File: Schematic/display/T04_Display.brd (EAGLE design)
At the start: 76.3 x 50.8 mm, 46 parts

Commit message: Reverified ERC/DRC for assignment files, added version summery.
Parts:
- C1, C10, C11, C12, C13, C14, C2, C3, C4, C5, C6, C7, C8, C9: value (none) -> 0.1u
- LED1, LED4, LED7: value (none) -> G
- LED2, LED5, LED8: value (none) -> Y
- LED3, LED6, LED9: value (none) -> R
- R1, R2, R3, R4, R5, R6, R7, R8, R9: value (none) -> 150

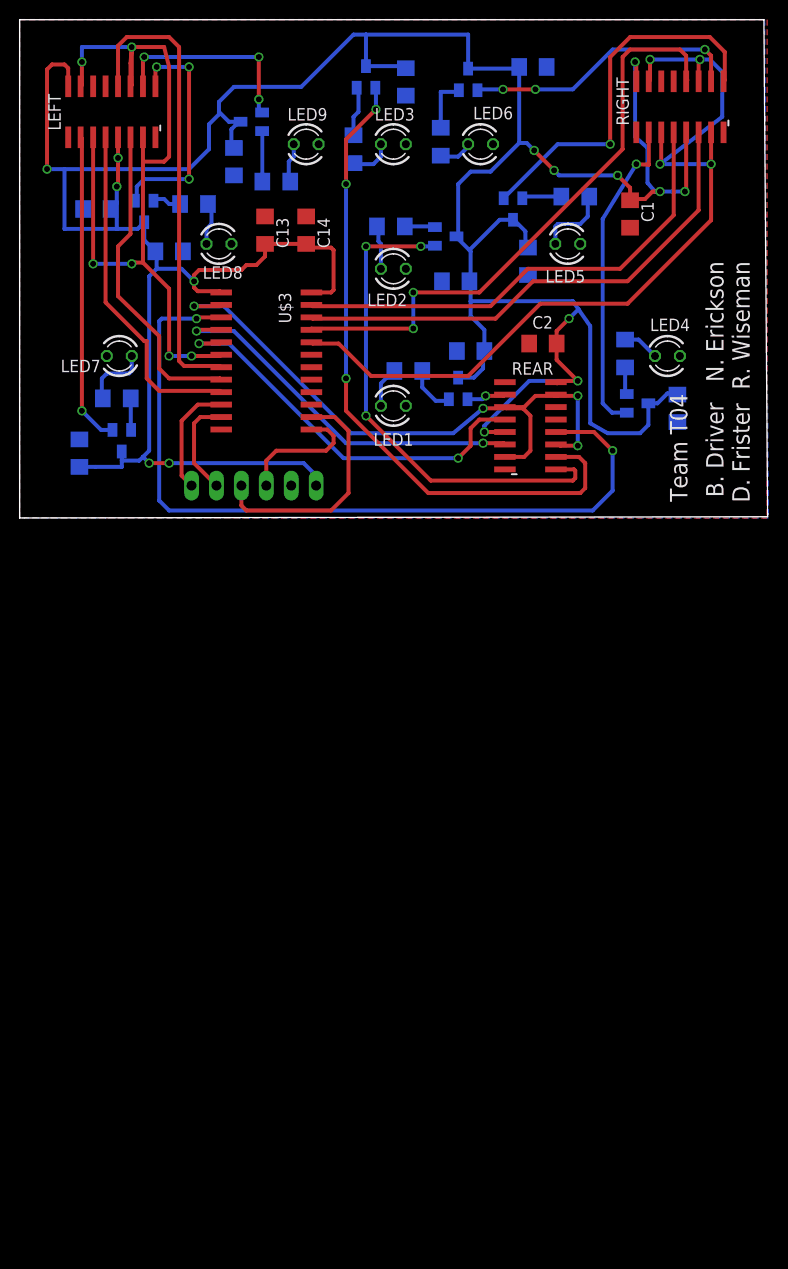
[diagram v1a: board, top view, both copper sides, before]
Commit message: Mainboard & Display layout updates - Molex connectors, Mounting Holes, Greenberg Email Additions
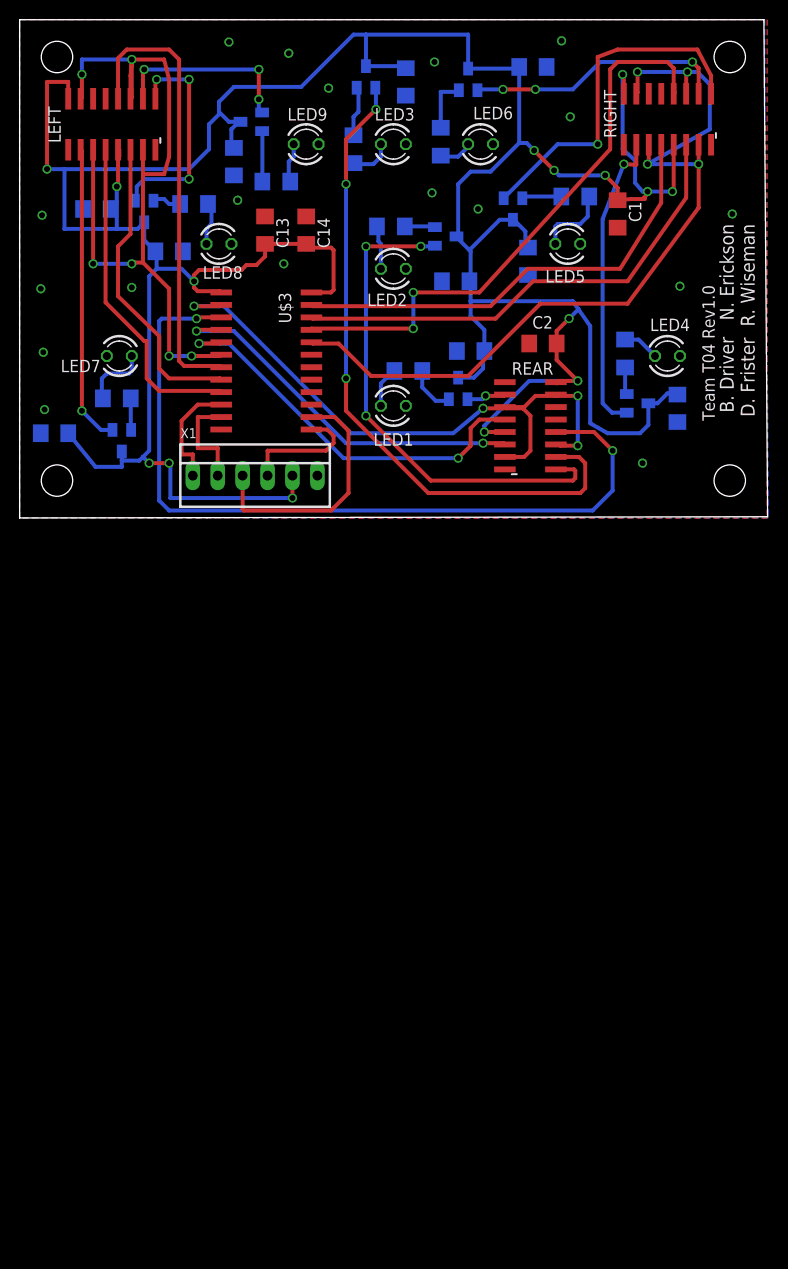
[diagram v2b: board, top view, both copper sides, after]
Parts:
- removed SV1: Connector, con-lstb:MA06-1
- added X1: (no value), con-molex:22-23-2061
- moved C12 3.25 mm to (3.56, 8.64), turned to 0 degrees
- moved RIGHT 1.80 mm to (66.0, 40.6)
- moved LEFT 1.27 mm to (9.40, 40.1)
- moved C1 1.27 mm to (61.0, 31.0)
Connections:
- net A0: now also X1.1; no longer SV1.6
- net A1: now also X1.2; no longer SV1.5
- net A2: now also X1.3; no longer SV1.4
- net A3: now also X1.4; no longer SV1.3
- net GND: now also X1.6; no longer SV1.2
- net VDD: now also X1.5; no longer SV1.1
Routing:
- net RRES: track 91.3 -> 86.9 mm
- net BRES: track 81.4 -> 78.7 mm
- net RS2: track 52.0 -> 49.7 mm
- net RS1: track 49.3 -> 46.9 mm
- net RY: track 38.2 -> 35.9 mm
- net RS3: track 60.8 -> 58.7 mm
- net RG: track 32.8 -> 30.9 mm
- net RR: track 28.4 -> 26.6 mm
- net VDD: track 348.9 -> 347.2 mm
- net BS1: track 34.6 -> 33.4 mm
- net BG: track 31.9 -> 30.6 mm
- net BS2: track 32.7 -> 31.4 mm
- net BR: track 20.5 -> 19.2 mm
- net BS3: track 47.7 -> 46.4 mm
- net BY: track 23.9 -> 22.7 mm
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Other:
- board text added: "Team T04 Rev1.0"
- board text removed: "Team T04"

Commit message: Updated Schematic and Revision text to match instructor review.
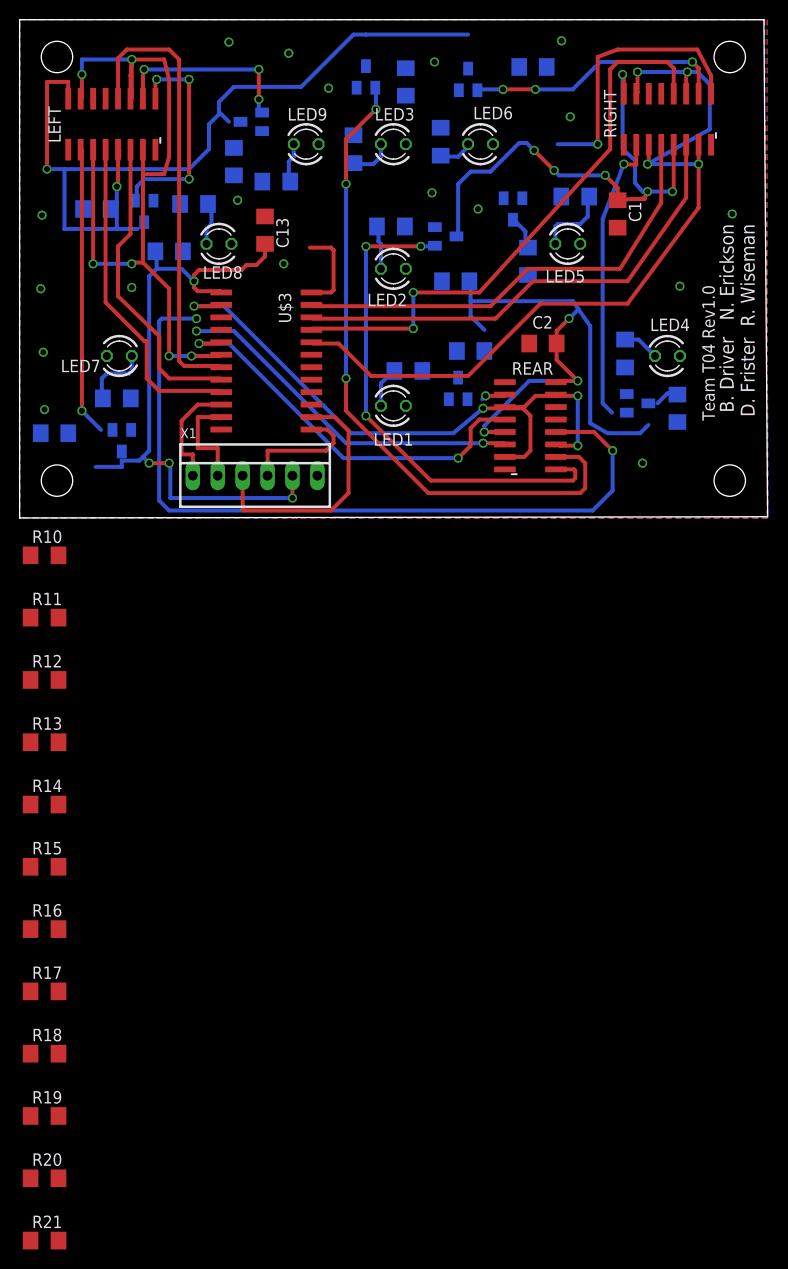
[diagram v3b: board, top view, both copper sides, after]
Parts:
- removed C14: 0.1u, resistor:C1206
- added R10, R11, R12, R13, R14, R15, R16, R17, R18, R19, R20, R21: 4700, rcl:R1206
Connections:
- removed net N$11: R7.2, U$9.2
- removed net N$2: R8.2, U$8.2
- removed net N$7: R9.2, U$6.2
- new net N$21: LED6.K, U$9.3
- new net N$22: LED4.K, U$6.3
- new net N$23: LED5.K, U$8.3
- net BRES: now also R18.2
- net BS1: now also R21.2
- net BS2: now also R20.2
- net BS3: now also R19.2
- net GND: now also R10.1, R11.1, R12.1, R13.1, R14.1, R15.1, R16.1, R17.1, R18.1, R19.1, R20.1, R21.1, U$1.2, U$10.2, U$12.2, U$13.2, U$4.2, U$5.2, U$6.2, U$8.2, U$9.2; no longer C14.1, LED1.K, LED2.K, LED3.K, LED4.K, LED5.K, LED6.K, LED7.K, LED8.K, LED9.K
- net LRES: now also R14.2
- net LS1: now also R17.2
- net LS2: now also R16.2
- net LS3: now also R15.2
- net N$1: now also LED3.K, U$5.3; no longer R5.2, U$4.2
- net N$13: now also LED7.K, U$10.3; no longer R1.2, U$10.2
- net N$15: now also LED8.K, U$12.3; no longer R2.2, U$12.2
- net N$17: now also LED9.K, U$13.3; no longer R3.2, U$13.2
- net N$3: now also LED2.K, U$4.3; no longer R6.2, U$5.2
- net N$4: now also LED1.K, U$1.3; no longer R4.2, U$1.2
- net RRES: now also R13.2
- net RS1: now also R10.2
- net RS2: now also R11.2
- net RS3: now also R12.2
- net VDD: now also R1.2, R2.2, R3.2, R4.2, R5.2, R6.2, R7.2, R8.2, R9.2; no longer C14.2, U$1.3, U$10.3, U$12.3, U$13.3, U$4.3, U$5.3, U$6.3, U$8.3, U$9.3
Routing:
- net VDD: track 347.2 -> 283.0 mm
- net RY: track 35.9 -> 28.1 mm
- net N$11: track 5.57 -> 0.00 mm
- net N$17: track 5.15 -> 0.00 mm
- net N$3: track 5.13 -> 0.00 mm
- net N$4: track 5.02 -> 0.00 mm
- net N$2: track 4.05 -> 0.00 mm
- net N$13: track 3.23 -> 0.00 mm
- net N$1: track 3.09 -> 0.00 mm
- net N$15: track 2.99 -> 0.00 mm
- net N$7: track 2.78 -> 0.00 mm
- net LS2: track 38.8 -> 36.4 mm
- net LS3: track 82.9 -> 80.5 mm
- net RG: track 30.9 -> 29.4 mm
- net LG: track 4.01 -> 2.50 mm
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
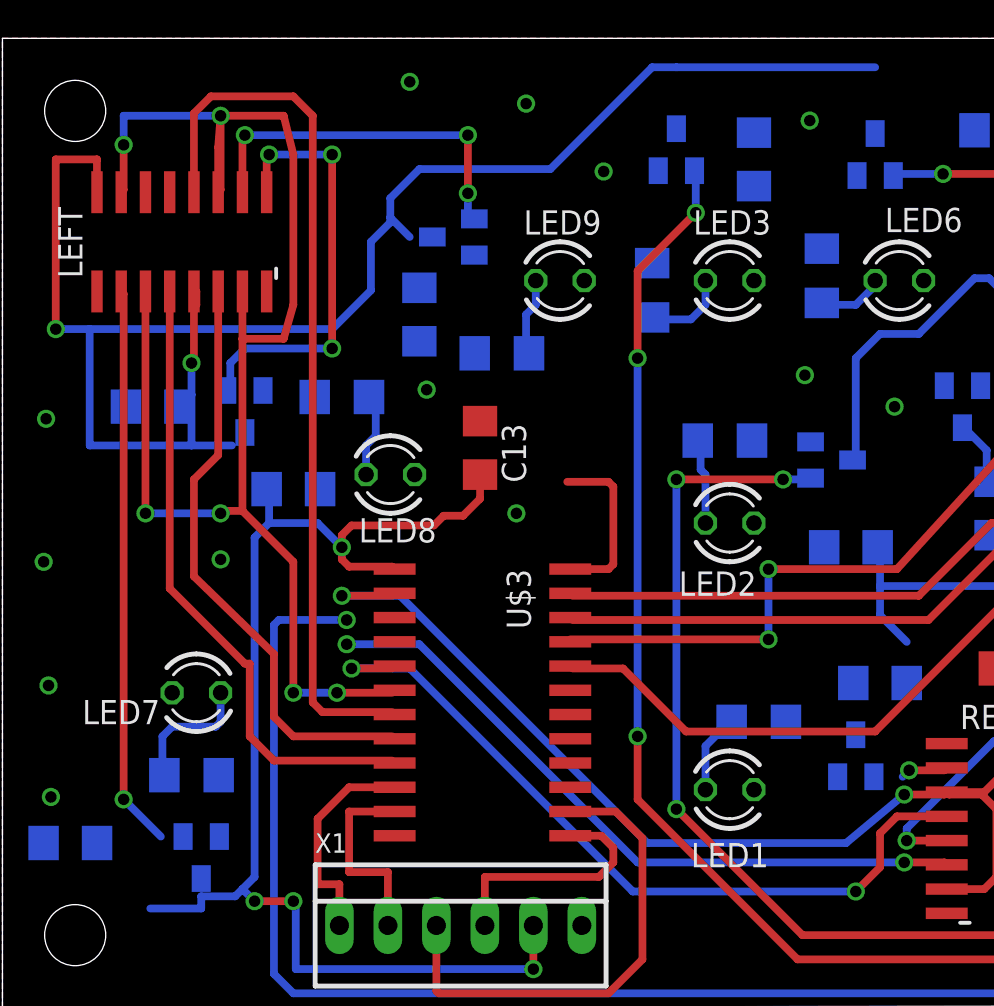
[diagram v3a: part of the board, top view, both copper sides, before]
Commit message: Updated display board
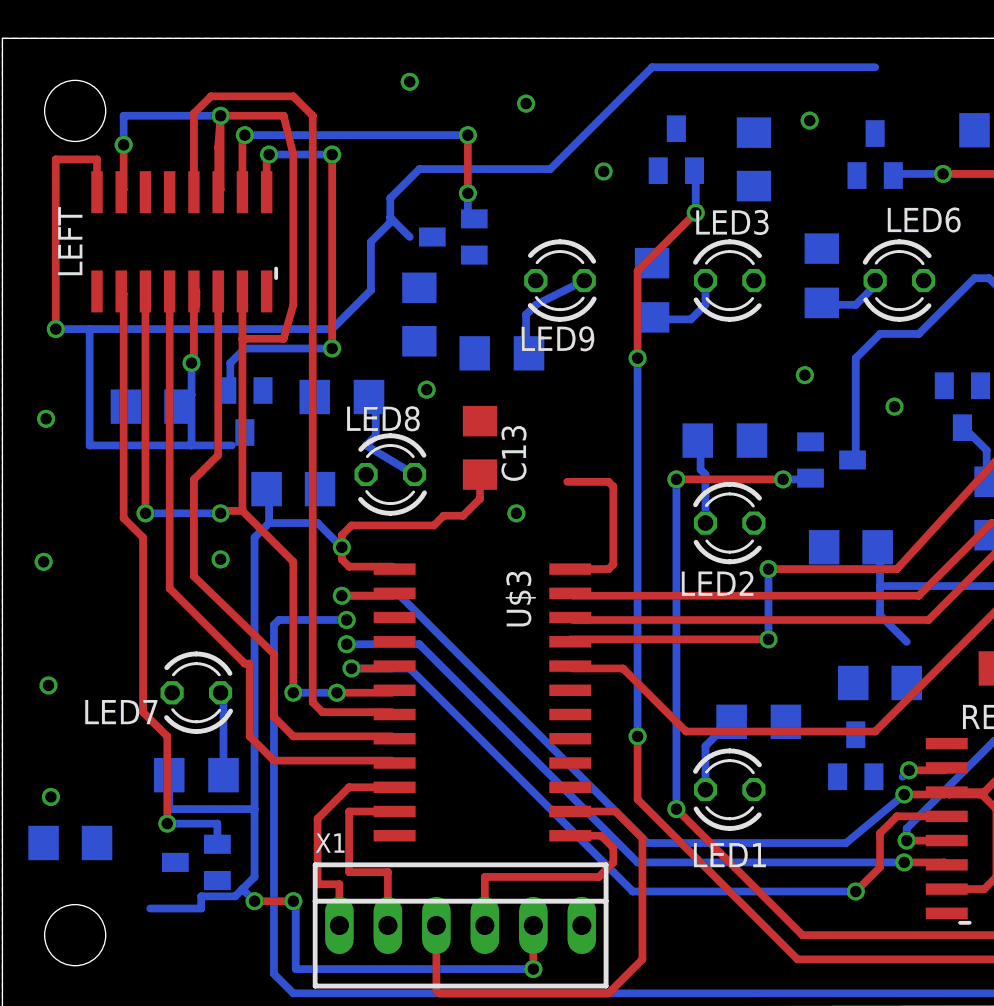
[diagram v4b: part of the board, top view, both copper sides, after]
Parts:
- moved U$10 0.36 mm to (10.2, 7.62), turned to 270 degrees
- moved R1 0.25 mm to (10.2, 12.2), turned to 0 degrees
- turned LED8 to 180 degrees
- turned LED9 to 180 degrees
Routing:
- net VDD: track 283.0 -> 289.3 mm
- net BG: track 29.4 -> 32.6 mm
- net N$14: track 6.96 -> 4.47 mm
- net N$18: track 4.08 -> 5.65 mm
- net N$16: track 4.42 -> 5.86 mm

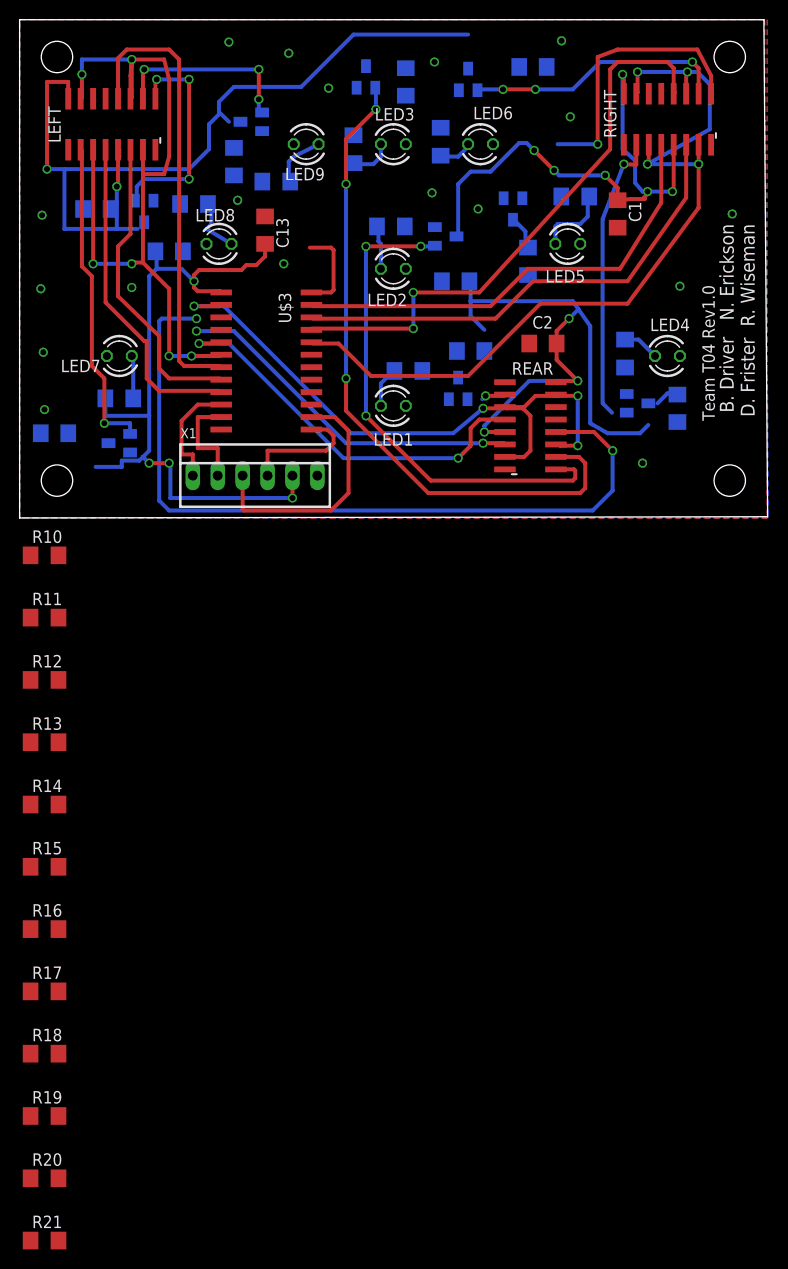
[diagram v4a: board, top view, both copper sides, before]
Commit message: Rev 1.5 of display board. Still needs updated mulex connector
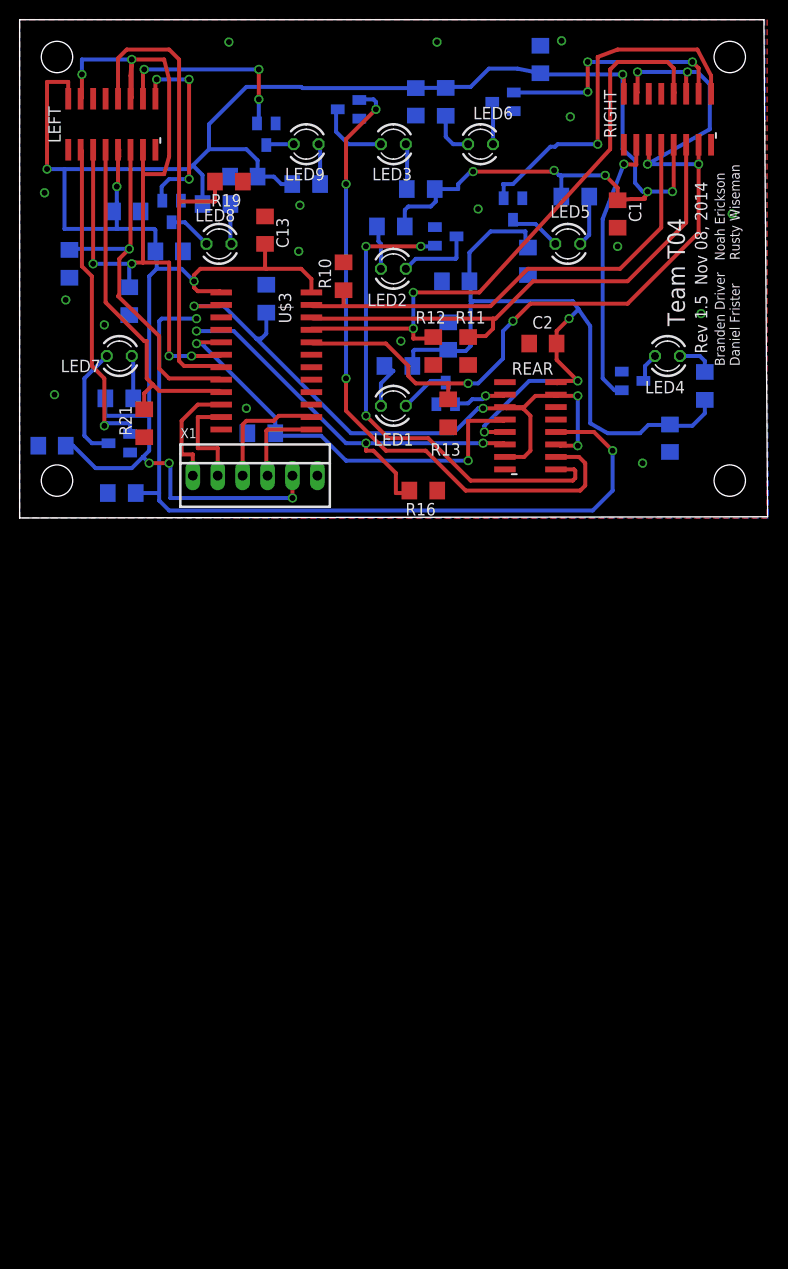
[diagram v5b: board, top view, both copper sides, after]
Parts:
- moved R19 97.1 mm to (21.3, 34.3), turned to 180 degrees
- moved R20 93.3 mm to (5.08, 25.9), flipped to the bottom, turned to 90 degrees
- moved R21 83.9 mm to (12.7, 9.65), turned to 90 degrees
- moved R18 77.2 mm to (11.2, 22.1), flipped to the bottom, turned to 90 degrees
- moved R17 61.0 mm to (24.6, 8.64), flipped to the bottom, turned to 180 degrees
- moved R16 59.1 mm to (41.1, 2.79), turned to 180 degrees
- moved R14 56.3 mm to (25.1, 22.4), flipped to the bottom, turned to 270 degrees
- moved R13 53.1 mm to (43.7, 10.7), turned to 90 degrees
- moved R12 51.9 mm to (42.2, 17.0), turned to 90 degrees
- moved R11 51.0 mm to (45.7, 17.0), turned to 90 degrees
- moved R10 41.7 mm to (33.0, 24.6), turned to 270 degrees
- moved R15 38.9 mm to (10.4, 2.54), flipped to the bottom, turned to 180 degrees
- moved R9 8.77 mm to (69.8, 13.5)
- moved R6 7.97 mm to (40.9, 33.5), turned to 180 degrees
- moved U$9 4.23 mm to (49.3, 42.4), turned to 270 degrees
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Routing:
- net VDD: track 289.3 -> 349.0 mm
- net A2: track 25.7 -> 12.6 mm
- net N$13: track 0.00 -> 11.8 mm
- net RY: track 28.1 -> 36.8 mm
- net LS2: track 36.4 -> 44.7 mm, vias 2 -> 3
- net N$3: track 0.00 -> 7.82 mm
- net N$1: track 0.00 -> 7.45 mm
- net BS2: track 31.2 -> 37.5 mm, vias 0 -> 1
- net BS3: track 46.3 -> 51.9 mm
- net N$23: track 0.00 -> 5.34 mm
- net N$4: track 0.00 -> 5.19 mm
- net RRES: track 86.7 -> 91.8 mm, vias 4 -> 6
- net RS2: track 49.5 -> 54.0 mm
- net N$15: track 0.00 -> 4.47 mm
- net N$21: track 0.00 -> 4.35 mm
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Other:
- board text added: "Branden Driver Noah Erickson Daniel Frister Rusty Wiseman"
- board text added: "Rev 1.5 Nov 08, 2014"
- board text added: "Team T04"
- board text removed: "B. Driver N. Erickson D. Frister R. Wiseman"
- board text removed: "Team T04 Rev1.0"
